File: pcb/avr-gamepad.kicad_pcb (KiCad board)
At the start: 2 copper layers, 55.8 x 44.3 mm, 37 parts, among them J1 Conn_01x08, J2 Conn_01x08, J3 Conn_01x08_Female, P1 USB_C_Plug_USB2.0, SW10 Up, SW11 Down, SW12 Left, SW13 Select, SW2 R, SW3 X, SW4 A, SW5 B, SW6 Start, SW7 Y, SW8 Right, SW9 L, U1 ATmega32U4-AU, Y1 Crystal_GND24

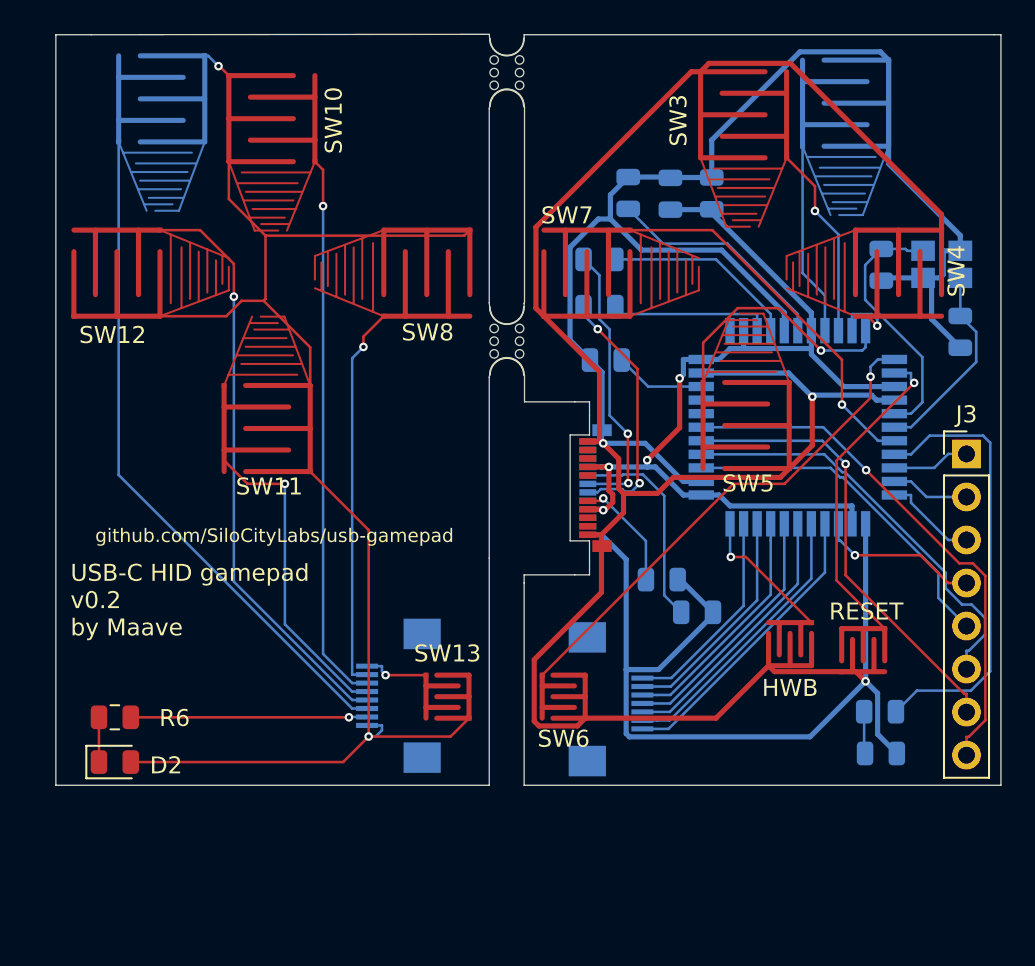
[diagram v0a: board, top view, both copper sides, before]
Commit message: tweak gamepad shell triggers, button holes, and faceplate pegs. 45 degree cut PCB corners. test add ffc connector for joystick
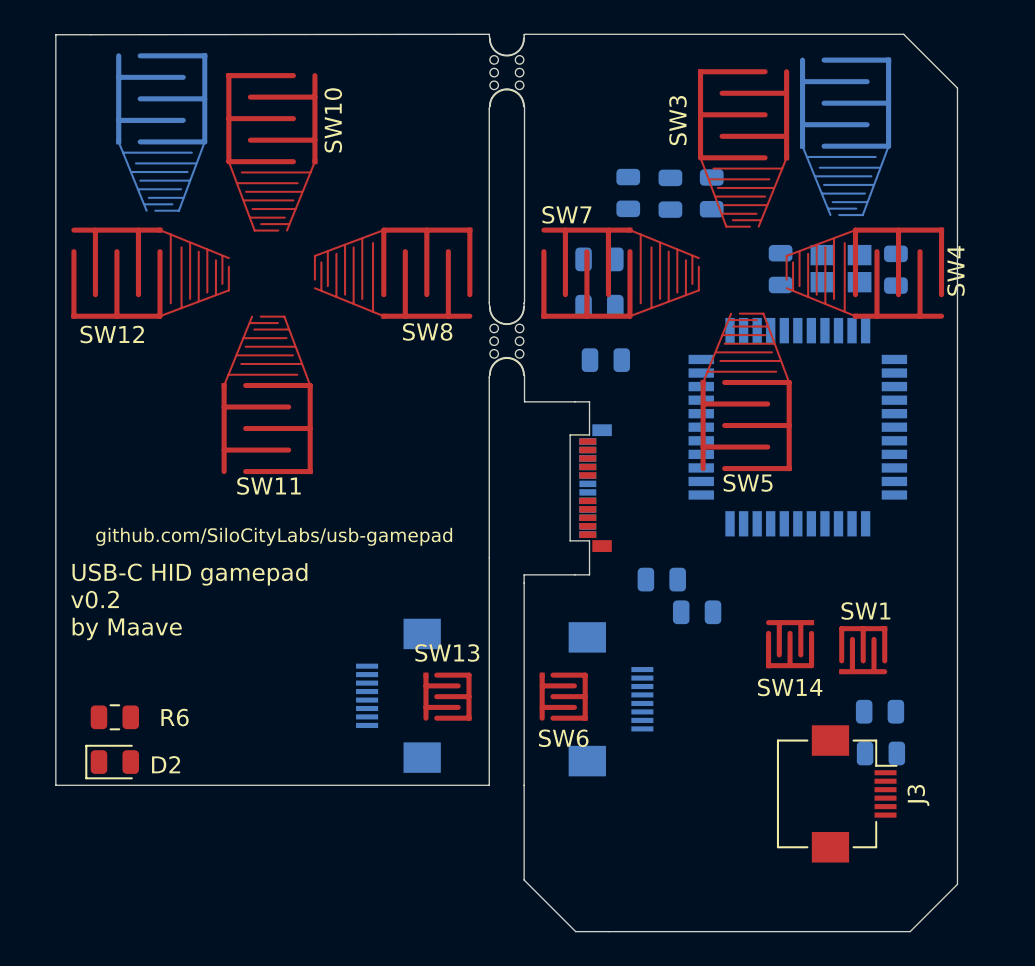
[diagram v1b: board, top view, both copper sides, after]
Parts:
- J3: value Conn_01x08_Female -> Conn_01x05; footprint Connector_PinHeader_2.54mm:PinHeader_1x08_P2.54mm_Vertical -> Connector_FFC-FPC:Hirose_FH12-6S-0.5SH_1x06-1MP_P0.50mm_Horizontal
- moved J3 21.1 mm to (146.9, 125.2), turned to 270 degrees
- moved Y1 5.95 mm to (146.2, 94.2)
- moved C4 5.95 mm to (142.6, 94.2)
- moved C3 5.28 mm to (149.4, 94.3), turned to 90 degrees
- renumbered RESET to SW1, HWB to SW14
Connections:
- J3 pad 1: /pd2-20 -> +5V
- J3 pad 2: /pd3-21 -> /pf7-36
- J3 pad 3: /pd5-22 -> /pd2-20
- J3 pad 4: /pd4-25 -> GND
- J3 pad 5: /pf7-36 -> /pf6-37
- J3 pad 6: /pf6-37 -> (no net)
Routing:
- net GND: track 252.6 -> 0.00 mm, vias 3 -> 0
- net Net-(D2-Pad2): track 91.3 -> 0.00 mm, vias 2 -> 0
- net +5V: track 58.9 -> 0.00 mm, vias 4 -> 0
- net Net-(J1-Pad6): track 40.0 -> 0.00 mm
- net Net-(J1-Pad5): track 34.7 -> 0.00 mm, vias 1 -> 0
- net Net-(J1-Pad3): track 32.6 -> 0.00 mm, vias 1 -> 0
- net /pf4-39: track 31.5 -> 0.00 mm, vias 1 -> 0
- net /pb7-12: track 29.6 -> 0.00 mm, vias 1 -> 0
- net /pf5-38: track 26.8 -> 0.00 mm, vias 1 -> 0
- net /pd1-19: track 26.3 -> 0.00 mm
- net /pf6-37: track 24.8 -> 0.00 mm
- net Net-(J1-Pad4): track 23.4 -> 0.00 mm, vias 1 -> 0
- net Net-(J1-Pad2): track 22.8 -> 0.00 mm, vias 1 -> 0
- net /pd0-18: track 22.3 -> 0.00 mm, vias 1 -> 0
- net /pf7-36: track 20.4 -> 0.00 mm
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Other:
- board size 55.8 x 44.3 mm -> 53.2 x 53 mm

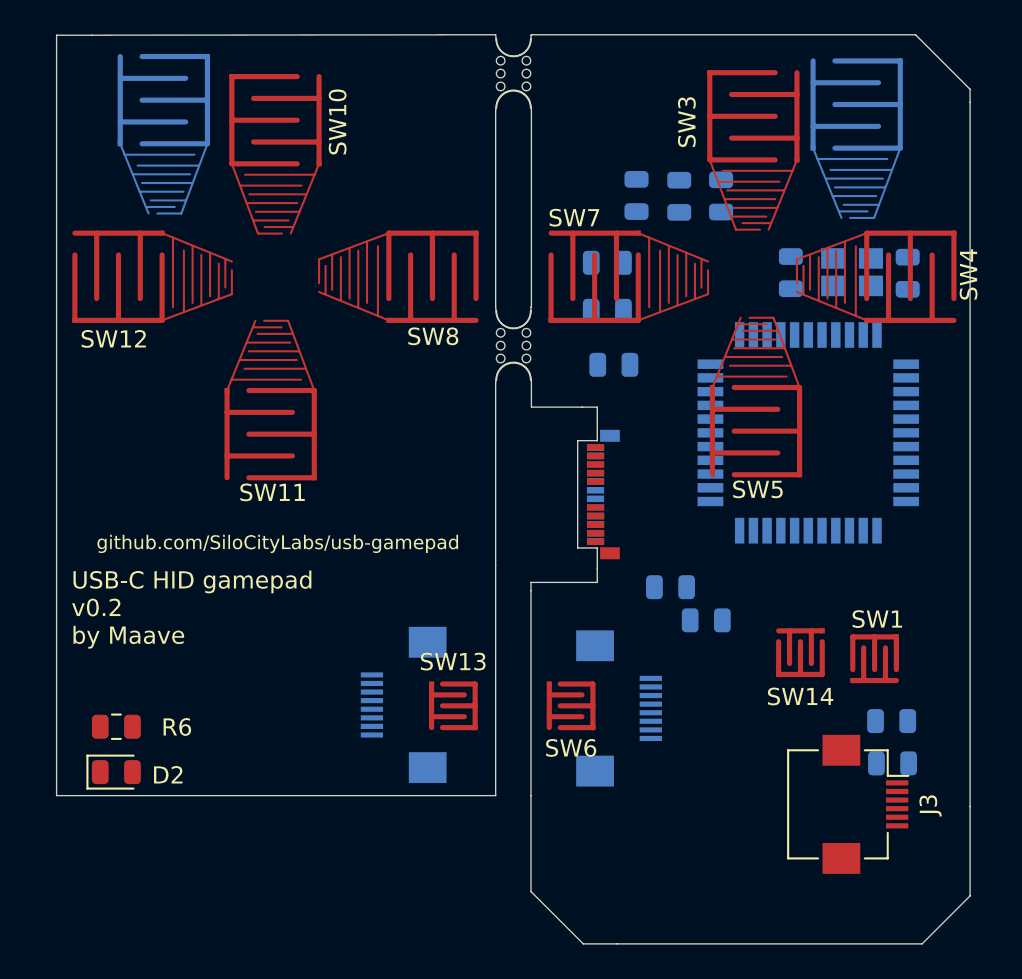
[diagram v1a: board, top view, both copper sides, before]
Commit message: actually add 45 degree corners
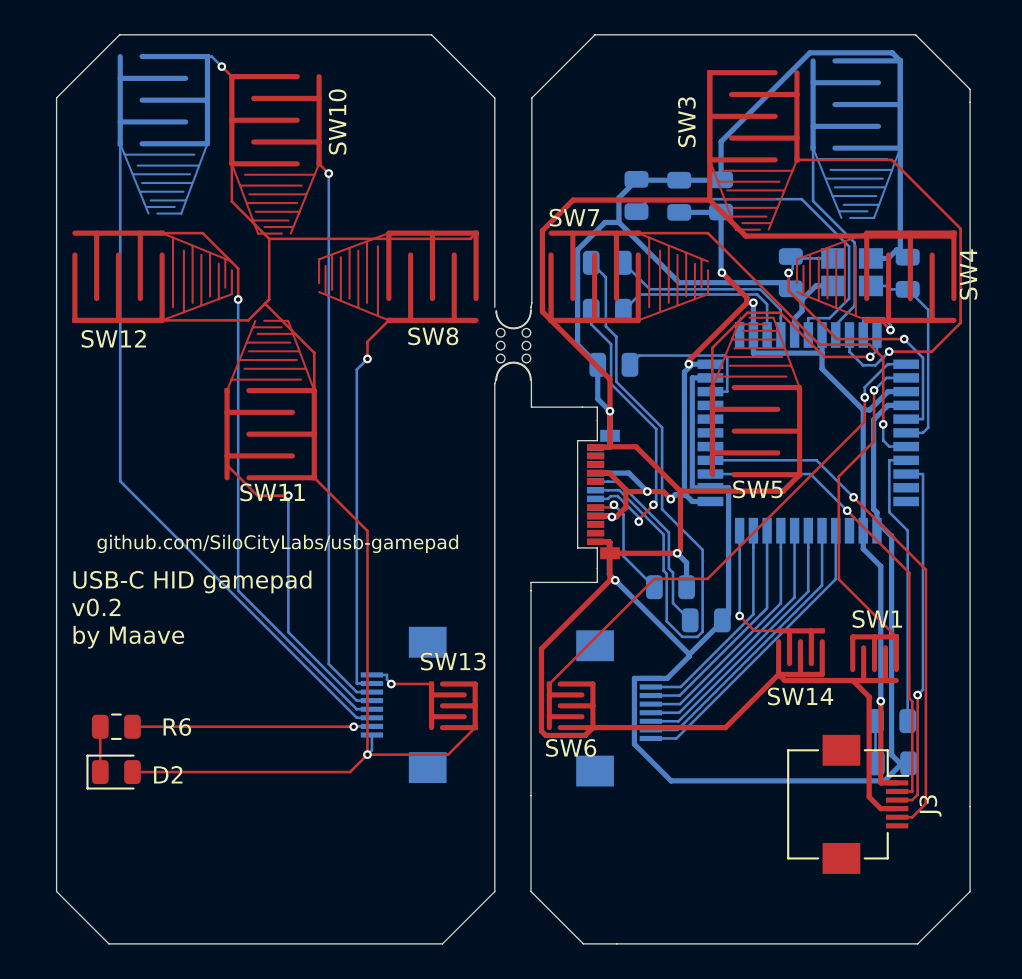
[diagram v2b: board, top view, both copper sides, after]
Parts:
- removed mb-2mm-1: mb1, Panelization:mouse-bite-2mm-slot
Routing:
- net GND: track 0.00 -> 260.7 mm, vias 0 -> 3
- net Net-(D2-Pad2): track 0.00 -> 90.8 mm, vias 0 -> 2
- net +5V: track 0.00 -> 76.1 mm, vias 0 -> 7
- net Net-(J1-Pad6): track 0.00 -> 40.0 mm
- net Net-(P1-PadA6): track 0.00 -> 36.9 mm
- net Net-(J1-Pad5): track 0.00 -> 34.7 mm, vias 0 -> 1
- net Net-(J1-Pad3): track 0.00 -> 32.6 mm, vias 0 -> 1
- net /pf6-37: track 0.00 -> 30.8 mm, vias 0 -> 1
- net /pb7-12: track 0.00 -> 29.7 mm, vias 0 -> 1
- net /pf7-36: track 0.00 -> 27.7 mm, vias 0 -> 1
- net /pb1-9: track 0.00 -> 25.5 mm, vias 0 -> 1
- net /pd0-18: track 0.00 -> 23.6 mm, vias 0 -> 1
- net Net-(J1-Pad4): track 0.00 -> 23.1 mm, vias 0 -> 1
- net Net-(J1-Pad2): track 0.00 -> 22.8 mm, vias 0 -> 1
- net /pd2-20: track 0.00 -> 21.1 mm, vias 0 -> 1
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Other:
- outline, holes or cut-outs redrawn

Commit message: cleanup schematic
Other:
- board text added: "USB-C HID gamepad v0.2 by Maave, ldrrp"
- board text added: "github.com/SiloCityLabs/Cuttlephone"
- board text removed: "USB-C HID gamepad v0.2 by Maave"
- board text removed: "github.com/SiloCityLabs/usb-gamepad"
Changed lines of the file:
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@@
-(kicad_pcb (version 20171130) (host pcbnew "(5.1.2)-1")
+(kicad_pcb (version 20171130) (host pcbnew 5.1.5-52549c5~86~ubuntu18.04.1)
   (general
     (thickness 0.1016)
@@
   )
   (layers
-    (0 F.Cu signal)
+    (0 F.Cu signal hide)
     (31 B.Cu signal)
-    (32 B.Adhes user)
-    (33 F.Adhes user)
+    (32 B.Adhes user hide)
+    (33 F.Adhes user hide)
     (34 B.Paste user hide)
     (35 F.Paste user hide)
-    (36 B.SilkS user)
-    (37 F.SilkS user)
-    (38 B.Mask user)
-    (39 F.Mask user)
-    (40 Dwgs.User user)
-    (41 Cmts.User user)
-    (42 Eco1.User user)
-    (43 Eco2.User user)
+    (36 B.SilkS user hide)
+    (37 F.SilkS user hide)
+    (38 B.Mask user hide)
+    (39 F.Mask user hide)
+    (40 Dwgs.User user hide)
+    (41 Cmts.User user hide)
+    (42 Eco1.User user hide)
+    (43 Eco2.User user hide)
     (44 Edge.Cuts user)
-    (45 Margin user)
-    (46 B.CrtYd user)
-    (47 F.CrtYd user)
+    (45 Margin user hide)
+    (46 B.CrtYd user hide)
+    (47 F.CrtYd user hide)
     (48 B.Fab user hide)
     (49 F.Fab user hide)
@@
   (gr_line (start 127.4572 124.714) (end 127.4572 130.302) (layer Edge.Cuts) (width 0.05))
   (gr_line (start 153.035 84.328) (end 153.035 125.349) (layer Edge.Cuts) (width 0.05))
-  (gr_text github.com/SiloCityLabs/usb-gamepad (at 112.7252 109.982) (layer F.SilkS)
+  (gr_text github.com/SiloCityLabs/Cuttlephone (at 112.2 109.982) (layer F.SilkS)
     (effects (font (size 0.8 0.8) (thickness 0.15)))
   )
-  (gr_text "USB-C HID gamepad\nv0.2\nby Maave" (at 100.6856 113.792) (layer F.SilkS)
+  (gr_text "USB-C HID gamepad\nv0.2\nby Maave, ldrrp" (at 100.6856 113.792) (layer F.SilkS)
     (effects (font (size 1 1) (thickness 0.15)) (justify left))
   )
